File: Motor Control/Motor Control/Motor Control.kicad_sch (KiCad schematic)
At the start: 10 parts, among them U1 DRV8833PW, U2 DRV8833PW

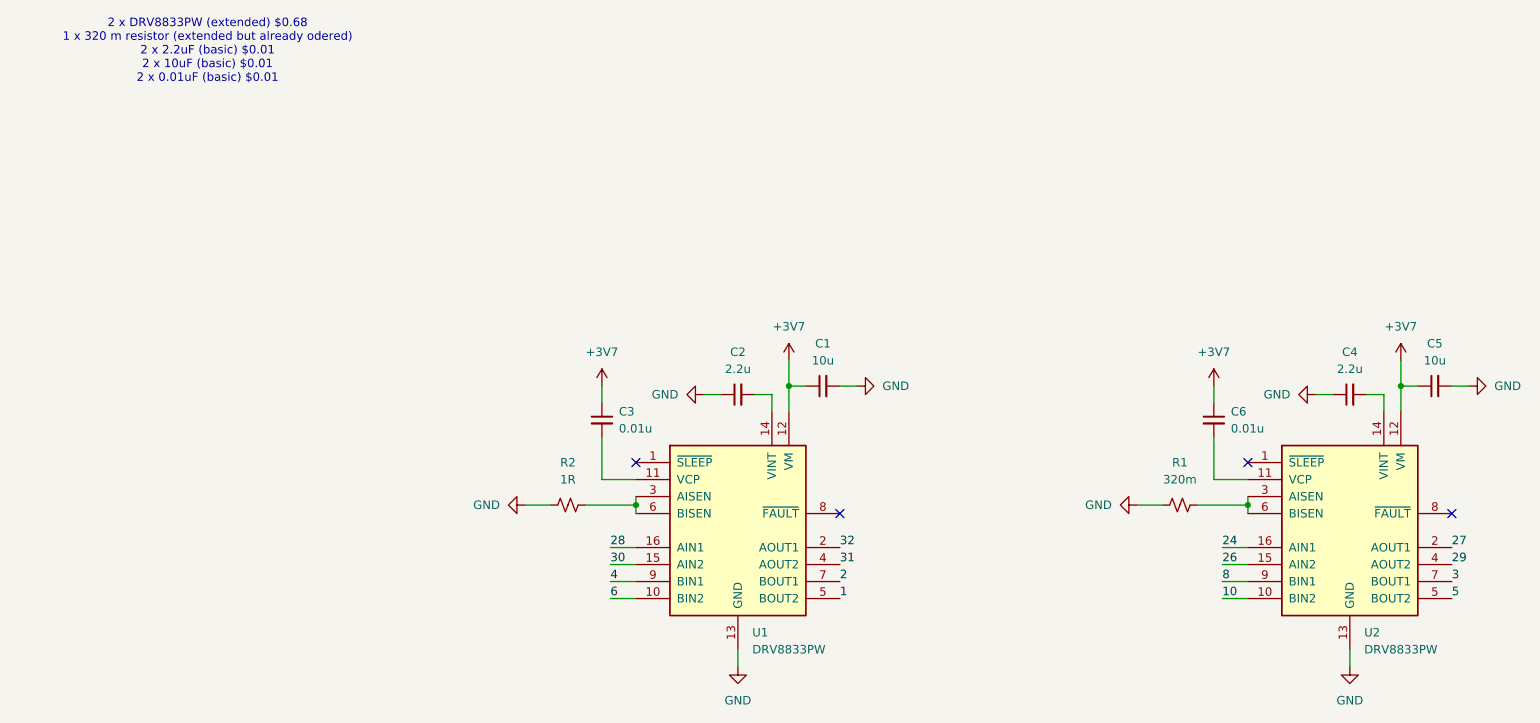
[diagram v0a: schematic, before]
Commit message: ON/OFF switch
Completed the ON/OFF switch.
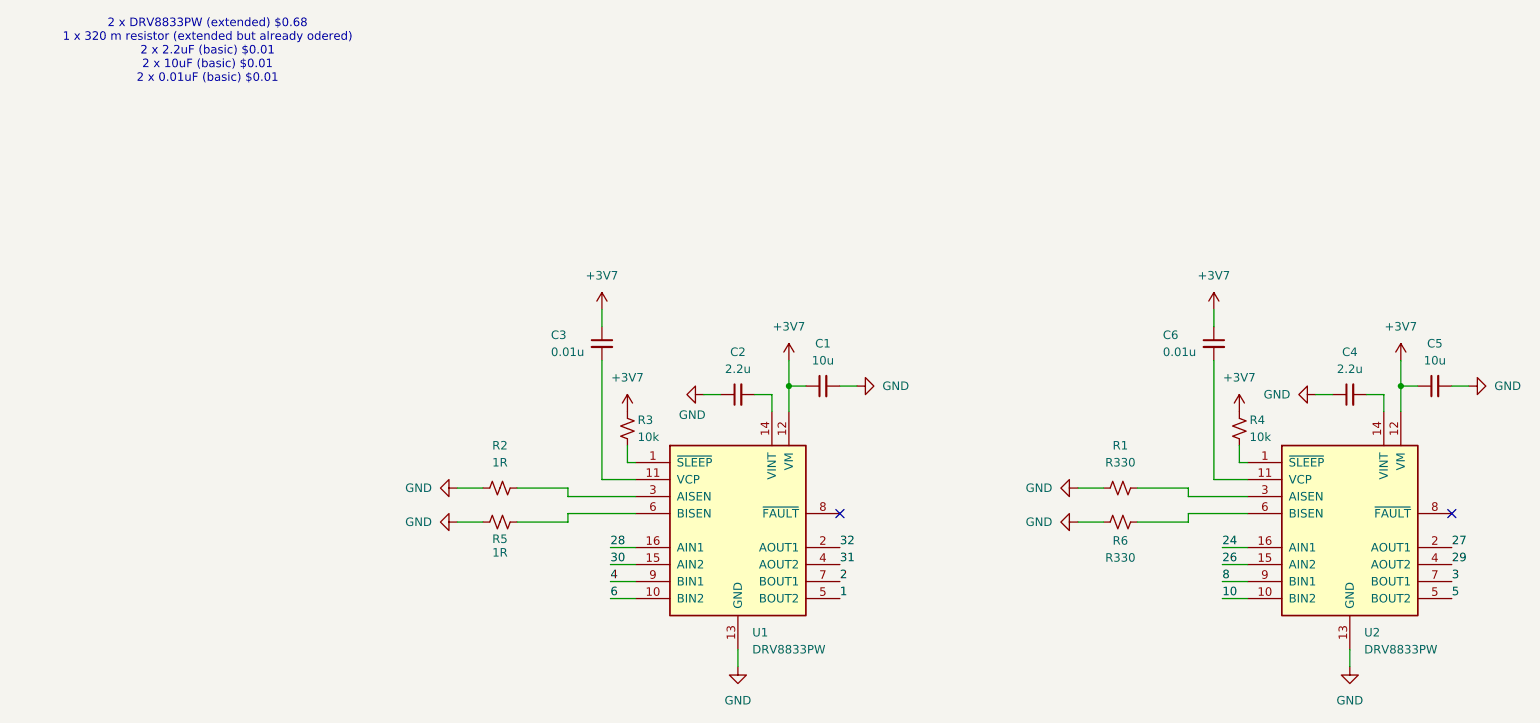
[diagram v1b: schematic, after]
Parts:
- added R3, R4: 10k, Resistor_SMD:R_0402_1005Metric_Pad0.72x0.64mm_HandSolder, symbol Device:R_Small_US
- added R5: 1R, Resistor_SMD:R_1206_3216Metric_Pad1.30x1.75mm_HandSolder, symbol Device:R_Small_US
- added R6: R330, Resistor_SMD:R_1206_3216Metric_Pad1.30x1.75mm_HandSolder, symbol Device:R_Small_US
- C1, C2, C4, C5: footprint (none) -> Capacitor_SMD:C_0402_1005Metric_Pad0.74x0.62mm_HandSolder
- C3, C6: footprint (none) -> Capacitor_SMD:C_0805_2012Metric_Pad1.18x1.45mm_HandSolder
- R1: value 320m -> R330; footprint (none) -> Resistor_SMD:R_1206_3216Metric_Pad1.30x1.75mm_HandSolder; LSCS (none) -> C25337
- R2: footprint (none) -> Resistor_SMD:R_1206_3216Metric_Pad1.30x1.75mm_HandSolder
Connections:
- net +3V7: now also R3.1, R4.1
- net GND: now also R5.1, R6.1
- net at R2.2, U1.3 (AISEN): no longer U1.6 (BISEN)
- net at U1.1 (~{SLEEP}): now also R3.2
- net at U2.1 (~{SLEEP}): now also R4.2
- net at R1.2, U2.3 (AISEN): no longer U2.6 (BISEN)
- new net: R5.2, U1.6 (BISEN)
- new net: R6.2, U2.6 (BISEN)
- no-connect marks 4 -> 2
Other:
- moved on the sheet: C3, R1, R2
